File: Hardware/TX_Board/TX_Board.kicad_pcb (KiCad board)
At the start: 2 copper layers, 153 x 131.5 mm, 198 parts, among them IC1 QPA9122TR7, IC10 QPA9122TR7, IC11 QPA9122TR7, IC2 MAPS-010164-TR0500, IC3 MAPS-010164-TR0500, IC4 QPA9122TR7, IC5 GP2Y1+, IC6 GP2Y1+, IC7 GP2Y1+, IC8 MAPS-010164-TR0500, IC9 MAPS-010164-TR0500, J1 Conn_Coaxial, J10 Conn_01x01_Pin, J11 Conn_Coaxial, J12 Conn_02x04_Odd_Even, J2 Conn_Coaxial, J3 Conn_Coaxial, J4 Conn_Coaxial, J5 Conn_02x08_Odd_Even, J6 Conn_01x03_Socket, J7 Conn_01x01_Pin, J8 Conn_01x01_Pin, J9 Conn_01x01_Pin, U1 SN74HCT138NSR, U2 LDO40LPU50RY, U3 ADP7182AUJZ-5.0

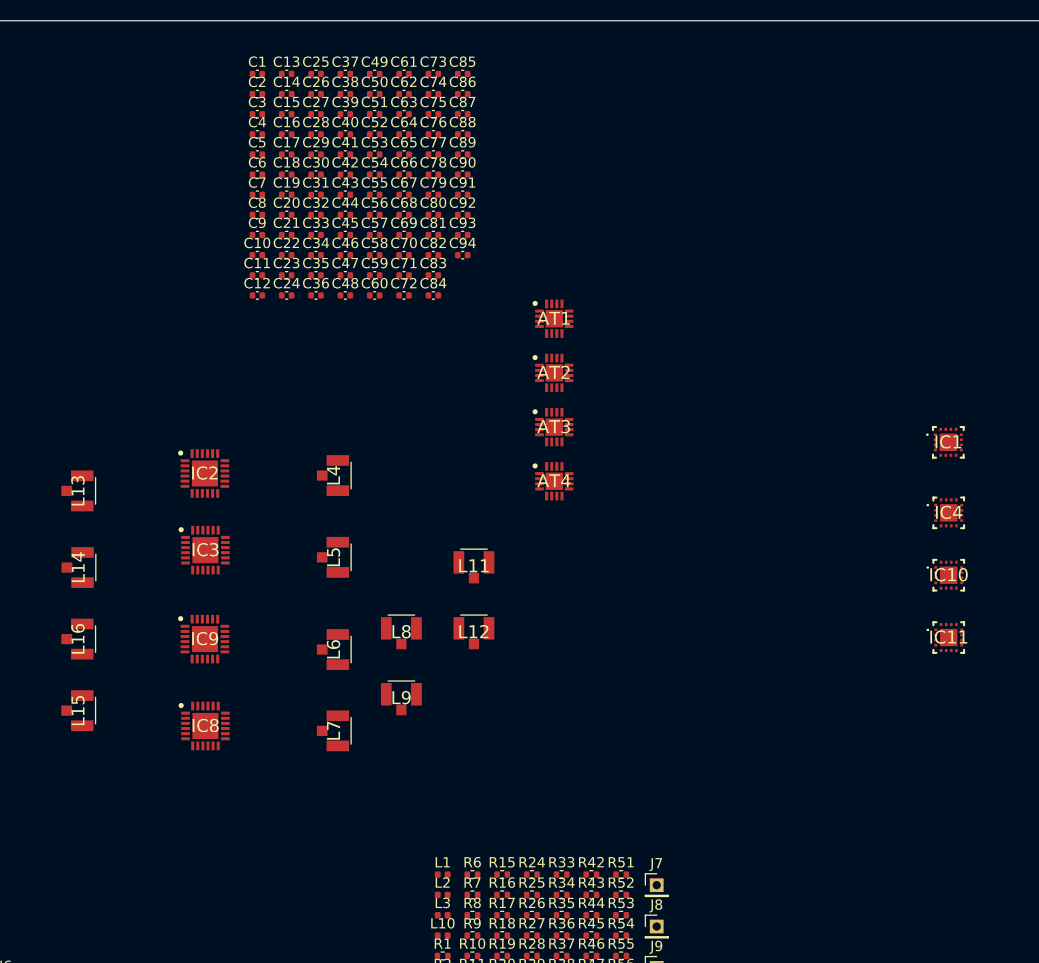
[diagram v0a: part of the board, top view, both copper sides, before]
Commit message: added LDO
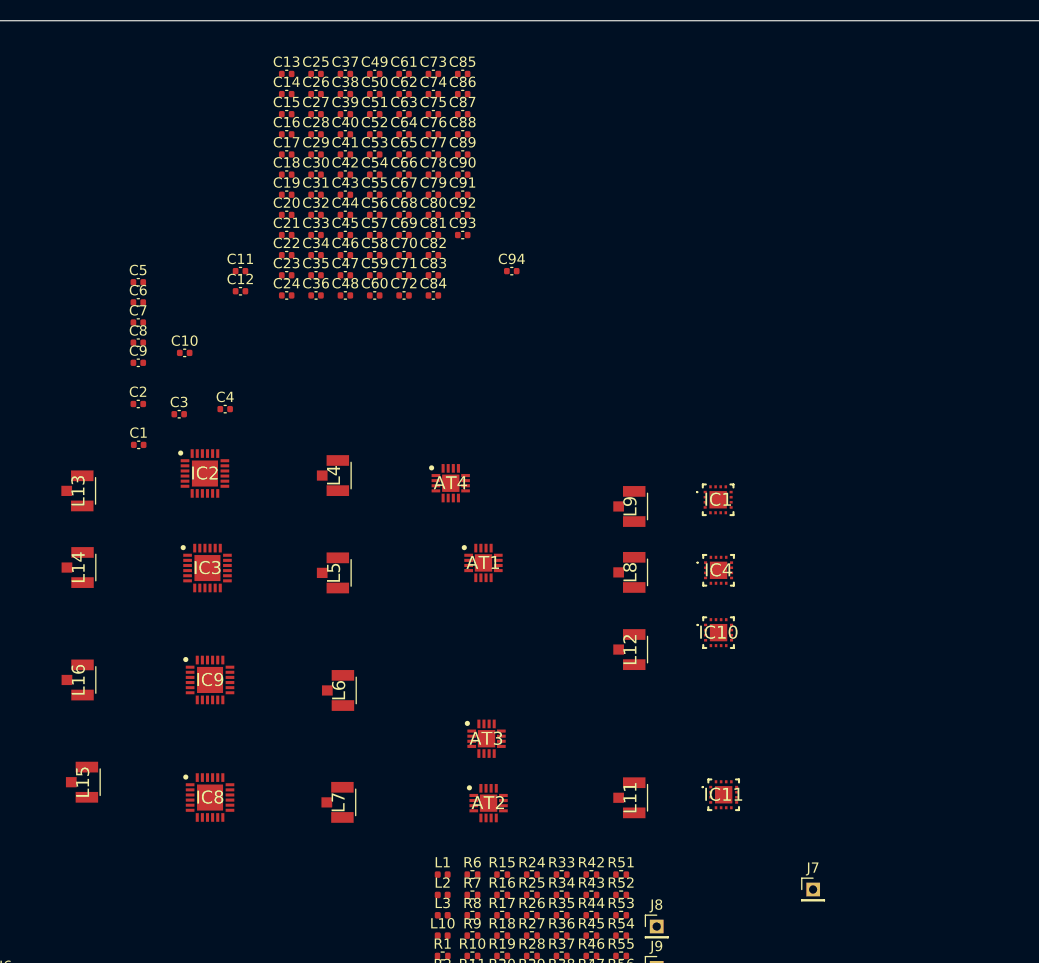
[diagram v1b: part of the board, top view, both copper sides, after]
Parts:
- moved AT2 42.6 mm to (130.8, 102.0)
- moved C1 38.1 mm to (96.5, 67.0)
- moved C2 32.5 mm to (96.5, 63.0)
- moved AT3 31.2 mm to (130.6, 95.8)
- moved C3 30.3 mm to (100.5, 64.0)
- moved L9 29.3 mm to (145.0, 73.0), turned to -90 degrees
- moved L11 27.9 mm to (145.0, 101.5), turned to -90 degrees
- moved C4 27.1 mm to (105.0, 63.5)
- moved IC11 26.9 mm to (153.8, 101.2)
- moved AT1 24.9 mm to (130.2, 78.5)
- moved L8 23.4 mm to (145.0, 79.5), turned to -90 degrees
- moved IC10 23.2 mm to (153.2, 85.4)
- moved IC4 23.2 mm to (153.2, 79.3)
- moved IC1 23.2 mm to (153.2, 72.4)
- moved C5 17.1 mm to (96.5, 51.1)
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
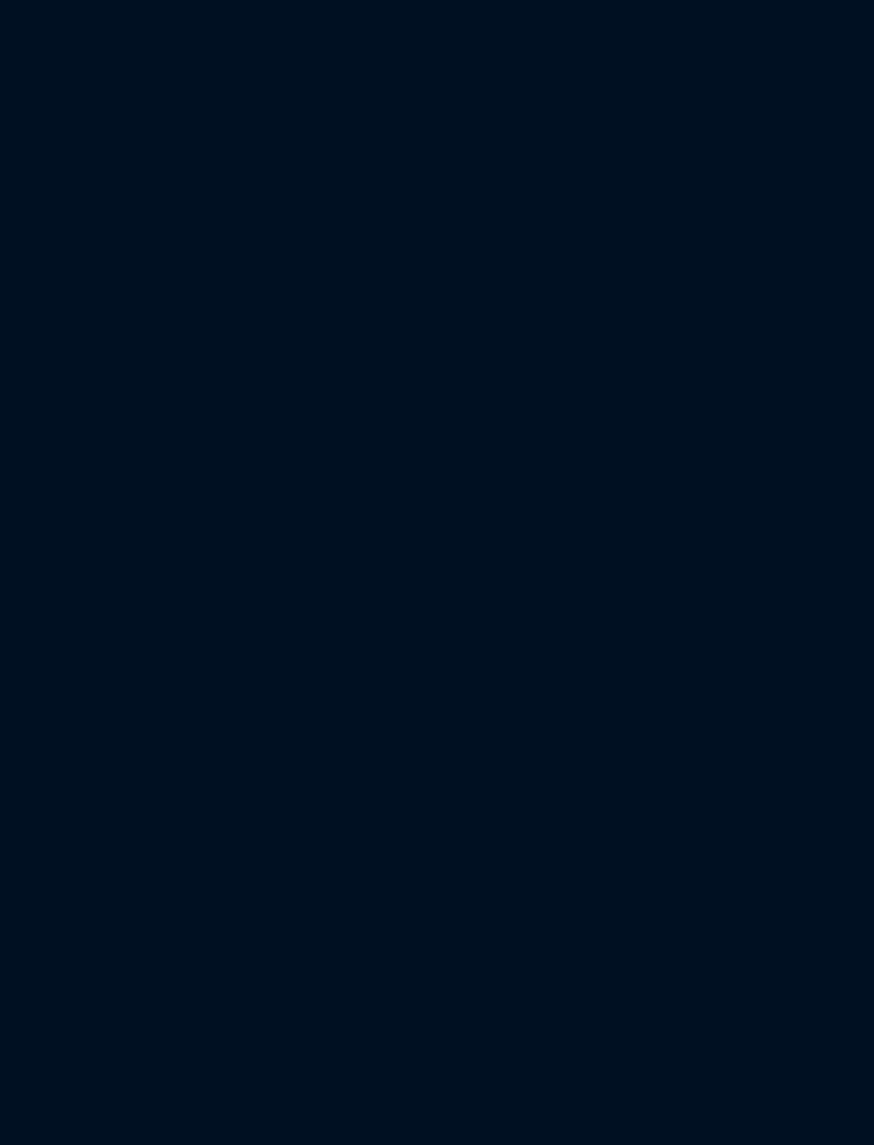
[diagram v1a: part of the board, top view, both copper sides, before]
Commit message: switched out UFL to SWG
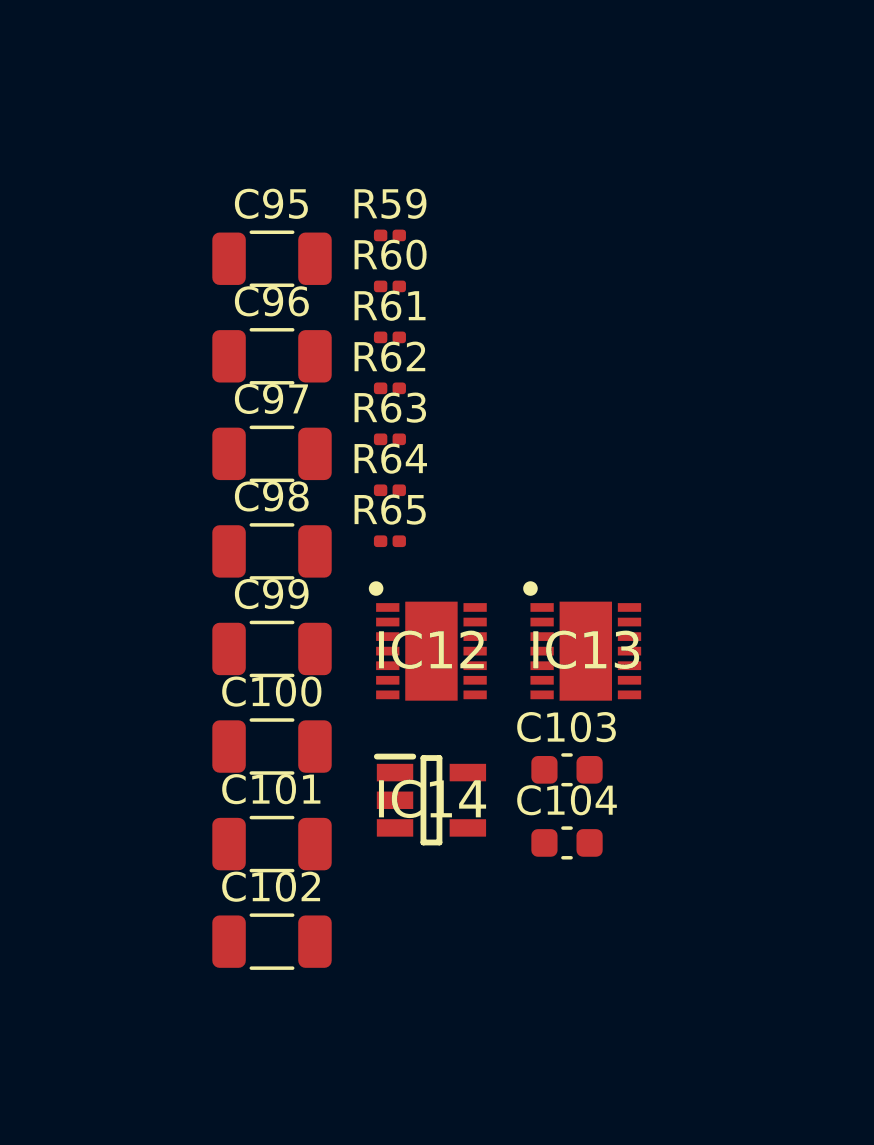
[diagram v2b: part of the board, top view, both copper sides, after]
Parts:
- added C100: 10uF, Capacitor_SMD:C_1206_3216Metric, F.Cu at (65.2, 52.3)
- added C101: 10uF, Capacitor_SMD:C_1206_3216Metric, F.Cu at (65.2, 55.6)
- added C102: 4.7uF, Capacitor_SMD:C_1206_3216Metric, F.Cu at (65.2, 59.0)
- added C103: 1uF, Capacitor_SMD:C_0603_1608Metric, F.Cu at (75.4, 53.1)
- added C104: 1uF, Capacitor_SMD:C_0603_1608Metric, F.Cu at (75.4, 55.6)
- added C95: 4.7uF, Capacitor_SMD:C_1206_3216Metric, F.Cu at (65.2, 35.5)
- added C96: 10uF, Capacitor_SMD:C_1206_3216Metric, F.Cu at (65.2, 38.9)
- added C97: 10uF, Capacitor_SMD:C_1206_3216Metric, F.Cu at (65.2, 42.2)
- added C98: 10uF, Capacitor_SMD:C_1206_3216Metric, F.Cu at (65.2, 45.6)
- added C99: 10uF, Capacitor_SMD:C_1206_3216Metric, F.Cu at (65.2, 48.9)
- added IC12: LT3041ADE#PBF, LT3041ADE:SON50P300X400X80-15N-D, F.Cu at (70.7, 49.0)
- added IC13: LT3099ADE#PBF, LT3099ADE:SON50P300X400X80-15N-D, F.Cu at (76.0, 49.0)
- added IC14: ADPL40502AUJZ-1.5-R7, ADPL40502:SOT95P280X100-5N, F.Cu at (70.7, 54.1)
- added R59: 49.9k, Resistor_SMD:R_0201_0603Metric, F.Cu at (69.3, 34.7)
- added R60: 49.9k, Resistor_SMD:R_0201_0603Metric, F.Cu at (69.3, 36.5)
- added R61: 453k, Resistor_SMD:R_0201_0603Metric, F.Cu at (69.3, 38.2)
- added R62: 200k, Resistor_SMD:R_0201_0603Metric, F.Cu at (69.3, 40.0)
- added R63: 49.9k, Resistor_SMD:R_0201_0603Metric, F.Cu at (69.3, 41.7)
- added R64: 453k, Resistor_SMD:R_0201_0603Metric, F.Cu at (69.3, 43.5)
- added R65: 49.9k, Resistor_SMD:R_0201_0603Metric, F.Cu at (69.3, 45.2)

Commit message: if i fuck up go back to this version
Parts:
- removed L11, L12, L13, L14, L15, L16, L4, L5, L6, L7, L8, L9: U.FL-R-SMT-1_60_, UFL_R_SMT1_1_60:UFLRSMT160
- added J13: MM8030-2610RJ3, MM8030:MM80302610RJ3, F.Cu at (90.5, 70.5)
- added J14: MM8030-2610RJ3, MM8030:MM80302610RJ3, F.Cu at (90.5, 86.5)
- added J15: MM8030-2610RJ3, MM8030:MM80302610RJ3, F.Cu at (90.5, 101.5)
- added J16: MM8030-2610RJ3, MM8030:MM80302610RJ3, F.Cu at (90.7, 117.5)
- added J17: MM8030-2610RJ3, MM8030:MM80302610RJ3, F.Cu at (115.5, 70.5)
- added J18: MM8030-2610RJ3, MM8030:MM80302610RJ3, F.Cu at (139.4, 70.5)
- added J19: MM8030-2610RJ3, MM8030:MM80302610RJ3, F.Cu at (115.5, 86.5)
- added J20: MM8030-2610RJ3, MM8030:MM80302610RJ3, F.Cu at (139.4, 86.5)
- added J21: MM8030-2610RJ3, MM8030:MM80302610RJ3, F.Cu at (115.5, 101.5)
- added J22: MM8030-2610RJ3, MM8030:MM80302610RJ3, F.Cu at (139.4, 101.5)
- added J23: MM8030-2610RJ3, MM8030:MM80302610RJ3, F.Cu at (115.5, 117.5)
- added J24: MM8030-2610RJ3, MM8030:MM80302610RJ3, F.Cu at (139.5, 117.5)
- moved C89 89.5 mm to (170.5, 117.5)
- moved C75 83.2 mm to (133.0, 117.5)
- moved C90 74.2 mm to (170.5, 101.5)
- moved C44 68.1 mm to (170.0, 87.0)
- moved C18 66.4 mm to (170.0, 71.0)
- moved C76 65.3 mm to (133.0, 101.5)
- moved J9 65.3 mm to (128.3, 180.7)
- moved L1 65.3 mm to (107.4, 171.6)
- moved L10 65.3 mm to (107.4, 177.5)
- moved L3 65.3 mm to (107.4, 175.5)
- moved R11 65.3 mm to (110.3, 181.5)
- moved R12 65.3 mm to (110.3, 183.5)
- moved R14 65.3 mm to (110.3, 187.5)
- moved R15 65.3 mm to (113.2, 171.6)
- moved R17 65.3 mm to (113.2, 175.5)
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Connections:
- C14 pad 2: Net-(IC1-RFIN) -> Net-(J18-IN)
- C37 pad 2: Net-(IC4-RFIN) -> Net-(J20-IN)
- C75 pad 2: Net-(IC10-RFIN) -> Net-(J24-IN)
- C76 pad 2: Net-(IC11-RFIN) -> Net-(J22-IN)
- IC2 pad 14: Net-(AT4-RFIN) -> Net-(IC2-RF_OUT)
- IC3 pad 14: Net-(AT1-RFIN) -> Net-(IC3-RF_OUT)
- IC6 pad 7: RF_IN2 -> Net-(IC6-PORT_1)
- IC6 pad 9: RF_IN1 -> Net-(IC6-PORT_2)
- IC7 pad 7: RF_IN4 -> Net-(IC7-PORT_1)
- IC7 pad 9: RF_IN3 -> Net-(IC7-PORT_2)
- IC8 pad 14: Net-(AT2-RFIN) -> Net-(IC8-RF_OUT)
- IC9 pad 14: Net-(AT3-RFIN) -> Net-(IC9-RF_OUT)
- R14 pad 2: PS_LE2 -> PS_LE_2
- R18 pad 2: ATTN_LE2 -> ATTN_LE_2
- R28 pad 2: PS_LE4 -> PS_LE_4
- R36 pad 2: ATTN_LE4 -> ATTN_LE_4
